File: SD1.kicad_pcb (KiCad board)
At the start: 2 copper layers, 176.1 x 41.3 mm, 236 parts, among them J101 HR861153C, J102 10118194-0001LF, J103 JST ZH 1.5mm 1x5, J107 FPC PMS, J301 PJ-102AH, J302 PJ-102AH, J303 Conn_01x02, J304 Conn_01x02, J401 Conn_01x11, J402 Conn_ARM_JTAG_SWD_10, J403 FTDI_TTL_Cable, J801 Conn_01x02, Q1 FDT86244, Q101 BSS138, Q102 PDTC114EU,115, Q301 DMMT5401, Q302 DMMT5401, Q801 DMMT5401, Q802 DMMT5401, SW103 Multidirection_Switch, SW401 PTS810, T1 HR051067, U102 ER-TFTM028-4, U103 CP2102N-A02-GQFN28R, U104 CC2652P, U105 W5500, U106 EKMC1691111, U107 MCP23017, U108 BME280, U109 SCD30, U2 TPS23753A, U3 TL431A, U301 110-102, U302 LMP91000, U4 TCMT1107, U501 TLV70018, U502 ADPD188BI, U503 Smoke Chamber, U601 CCS811, U701 TPS61022, U702 TLV62585, Y101 25MHz

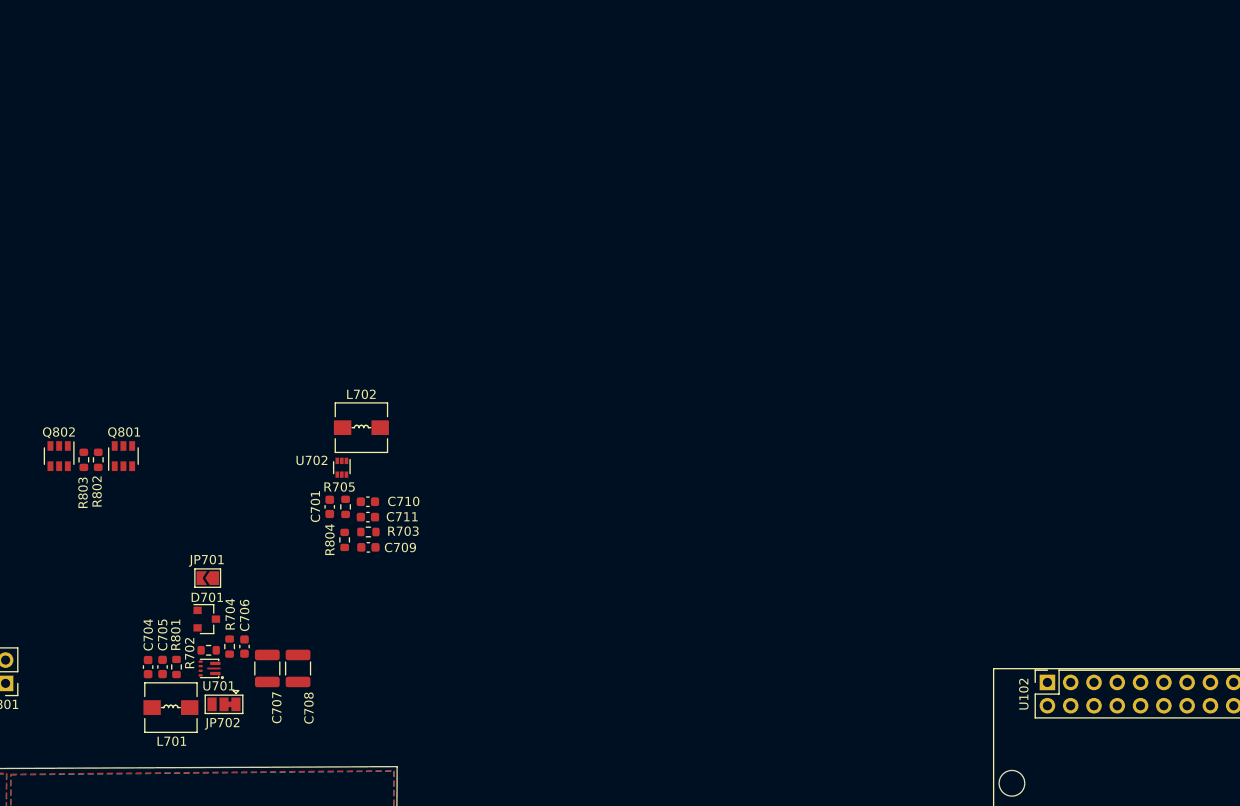
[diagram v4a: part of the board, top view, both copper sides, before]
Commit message: 5V boost and 3.3V buck layout
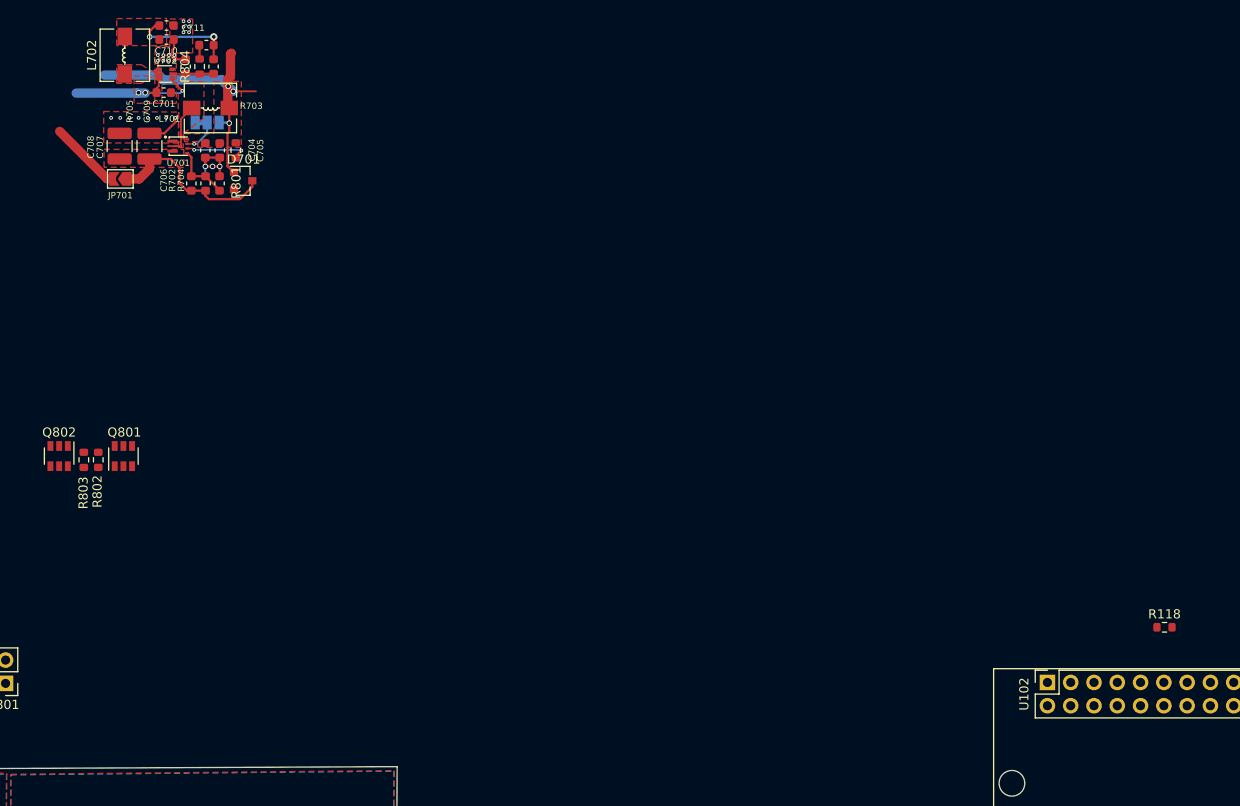
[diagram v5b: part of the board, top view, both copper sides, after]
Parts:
- added R118: 100k, Resistor_SMD:R_0603_1608Metric, F.Cu at (363.9, 42.6)
- JP702: moved to B.Cu
- moved L701 65.5 mm to (259.8, -14.0), turned to 180 degrees
- moved JP702 63.5 mm to (259.5, -12.5), turned to 0 degrees
- moved C708 60.2 mm to (249.9, -9.88), turned to 90 degrees
- moved C707 58.4 mm to (253.2, -9.88), turned to 90 degrees
- moved C711 57.9 mm to (255.0, -23.0), turned to 0 degrees
- moved U701 57.1 mm to (256.3, -9.88), turned to 0 degrees
- moved R801 56.7 mm to (262.6, -9.42), turned to 90 degrees
- moved C704 56.7 mm to (259.3, -9.42), turned to 270 degrees
- moved C705 56.7 mm to (260.9, -9.42), turned to 270 degrees
- moved R703 56.0 mm to (259.4, -20.9)
- moved C709 55.1 mm to (260.2, -18.6), turned to 270 degrees
- moved C710 55.0 mm to (255.0, -21.5), turned to 0 degrees
- moved R804 54.0 mm to (258.7, -18.6)
- moved R705 51.1 mm to (257.1, -18.6), turned to 270 degrees
- moved R702 50.9 mm to (259.3, -5.81), turned to 270 degrees
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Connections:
- U102 pad 29: (no net) -> /LCD_BACKLIGHT
- U102 pad 35: (no net) -> /SD_CS
- U107 pad 1: (no net) -> /SD_CS
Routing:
- net (no net): track 0.00 -> 112.8 mm
- net +BATT: track 0.00 -> 32.3 mm, vias 0 -> 3
- net /Power/5VOUT_BST: track 0.00 -> 19.5 mm
- net GND: track 154.9 -> 171.7 mm, vias 12 -> 37
- net +5V: track 29.8 -> 46.5 mm, vias 0 -> 3
- net +3V3: track 74.7 -> 86.2 mm, vias 3 -> 5
- net Net-(JP701-Pad2): track 0.00 -> 7.81 mm
- net /Power/EN_5V_BST: track 0.00 -> 7.13 mm, vias 0 -> 2
- net Net-(C706-Pad2): track 0.00 -> 6.47 mm
- net /Power/VSW: track 0.00 -> 5.38 mm
- net Net-(C709-Pad2): track 0.00 -> 4.61 mm
- net Net-(JP702-Pad2): track 0.00 -> 3.83 mm, vias 0 -> 1
- net Net-(R703-Pad2): track 0.00 -> 1.57 mm
- added copper zone on F.Cu, net (none)
- added copper zone on F.Cu, net +3V3
- added copper zone on F.Cu, net +BATT
- added copper zone on F.Cu, net /Power/5VOUT_BST
- added copper zone on F.Cu, net /Power/VSW
- added copper zone on F.Cu, net Net-(L702-Pad1)

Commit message: Add resistor to battery indicator, battery layout, update font sizes
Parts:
- added C801: 4.7u, Capacitor_SMD:C_0603_1608Metric, F.Cu at (199.5, 45.2)
- added C802: 4.7u, Capacitor_SMD:C_0603_1608Metric, F.Cu at (192.9, 43.2)
- added D801: LED_ALT, LED_SMD:LED_0603_1608Metric, F.Cu at (195.6, 39.9)
- added D802: LED_ALT, LED_SMD:LED_0603_1608Metric, F.Cu at (195.6, 38.3)
- added J802: Conn_01x02, Connector_JST:JST_PH_B2B-PH-K_1x02_P2.00mm_Vertical, F.Cu at (188.8, 44.2)
- added JP103: Jumper_3_Open, Connector_PinHeader_2.54mm:PinHeader_1x03_P2.54mm_Vertical, F.Cu at (134.2, 178.9)
- added JP801: Jumper_NO_Small, Jumper:SolderJumper-2_P1.3mm_Open_TrianglePad1.0x1.5mm, F.Cu at (203.0, 44.6)
- added R805: 1k, Resistor_SMD:R_0603_1608Metric, F.Cu at (195.6, 36.7)
- added R806: 10k, Resistor_SMD:R_0603_1608Metric, F.Cu at (199.5, 40.0)
- added R807: 1k, Resistor_SMD:R_0603_1608Metric, F.Cu at (198.7, 38.3)
- added U801: MCP73831-2-OT, Package_TO_SOT_SMD:SOT-23-5, F.Cu at (199.1, 42.6)
- moved J801 50.3 mm to (188.4, 37.9), turned to 90 degrees
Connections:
- net /Eth + PoE/PoE Flyback/5V_Main renamed 5V_Main
- Q102 pad 1: (no net) -> /SPKR_Alt
- R109 pad 1: (no net) -> /SPKR
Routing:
- net +BATT: track 32.3 -> 49.9 mm
- net 5V_Main: track 18.4 -> 32.7 mm, vias 2 -> 4
- net Net-(D801-Pad2): track 0.00 -> 5.61 mm
- net Net-(D802-Pad2): track 0.00 -> 2.44 mm
- net Net-(D801-Pad1): track 0.00 -> 2.25 mm
- net Net-(R806-Pad1): track 0.00 -> 1.69 mm
- net Net-(C801-Pad1): track 0.00 -> 1.63 mm

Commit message: Merge layout for PoE and Ethernet
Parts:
- removed MK109, MK110, MK111, MK112: Mounting_Hole_PAD, mylib:MountingHole_3.2mm_M3_ISO14580_Pad
- added D305: BAS16, Diode_SMD:D_SOT-23_ANK, F.Cu at (138.8, 23.2)
- added D306: BAS16, Diode_SMD:D_SOT-23_ANK, F.Cu at (138.8, 26.8)
- added J104: JST 1.25mm, Connector_Molex:Molex_PicoBlade_53398-0871_1x08-1MP_P1.25mm_Vertical, F.Cu at (195.2, 148.8)
- J107: value FPC PMS -> JST 1.25mm
- moved MK101 199.0 mm to (122.8, 10.8)
- moved R807 108.5 mm to (294.1, -13.4)
- moved C801 108.5 mm to (294.9, -6.50)
- moved C802 108.5 mm to (288.3, -8.50)
- moved D801 108.5 mm to (291.0, -11.8)
- moved J801 108.5 mm to (283.8, -13.8)
- moved JP801 108.5 mm to (298.4, -7.10)
- moved R805 108.5 mm to (291.0, -15.0)
- moved R806 108.5 mm to (294.9, -11.7)
- moved U801 108.5 mm to (294.5, -9.10)
- moved J802 108.5 mm to (284.2, -7.50)
- moved D802 108.5 mm to (291.0, -13.4)
- moved C101 105.8 mm to (203.8, 20.3)
- moved C102 105.8 mm to (203.8, 18.7)
- moved D101 105.8 mm to (201.4, 15.0)
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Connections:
- D301 pad 2: /Eth + PoE/PoE Flyback/DC_BARREL -> /Eth + PoE/PoE Flyback/DC_FROM_AC
- D302 pad 2: /Eth + PoE/PoE Flyback/DC_BARREL -> /Eth + PoE/PoE Flyback/DC_FROM_AC
- J301 pad 1: /Eth + PoE/PoE Flyback/DC_BARREL -> /Eth + PoE/PoE Flyback/DC_FROM_AC
- R303 pad 1: /Eth + PoE/PoE Flyback/DC_BARREL -> Net-(D305-Pad1)
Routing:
- net /Eth + PoE/PoE Flyback/VN: track 15.1 -> 55.6 mm
- net /Eth + PoE/PoE Flyback/VP: track 25.9 -> 56.8 mm
- net Net-(D305-Pad1): track 0.00 -> 18.7 mm, vias 0 -> 2
- net /Eth + PoE/PoE Flyback/DC_BARREL: track 0.00 -> 16.6 mm
- net +BATT: track 49.9 -> 36.3 mm, vias 3 -> 1
- net /Eth + PoE/PoE Flyback/DC_FROM_AC: track 0.00 -> 12.0 mm
- net Net-(JP701-Pad2): track 7.81 -> 0.50 mm
- net +5V: track 46.5 -> 39.8 mm
- net /Eth + PoE/ETH_TX_N: track 19.1 -> 24.7 mm
- net /DIO12_RXD: track 27.1 -> 21.7 mm
- net /Eth + PoE/ETH_RX_N: track 29.2 -> 33.5 mm
- net /Eth + PoE/ETH_RX_P: track 32.0 -> 35.8 mm
- net /Eth + PoE/PoE Flyback/APD: track 7.18 -> 5.37 mm, vias 2 -> 1
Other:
- board size 176.1 x 41.3 mm -> 292.9 x 89.5 mm

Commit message: 4layer layout WIP
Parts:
- removed J401: Conn_01x11, Connector_Molex:Molex_SL_171971-0011_1x11_P2.54mm_Vertical
- C802, JP101, JP102: moved to B.Cu
- moved R123 203.1 mm to (97.8, 57.4), turned to 180 degrees
- moved C115 192.3 mm to (88.8, 52.2), turned to 270 degrees
- moved C114 191.5 mm to (210.0, 76.8), turned to 180 degrees
- moved JP401 188.3 mm to (213.4, 18.6), turned to 180 degrees
- moved U109 182.5 mm to (211.0, 74.4), turned to 180 degrees
- moved MK102 169.6 mm to (217.2, 10.8)
- moved SW103 160.1 mm to (122.8, 65.0)
- moved R118 158.0 mm to (212.6, 88.0), turned to 90 degrees
- moved D501 145.6 mm to (139.8, 104.9), turned to 105 degrees
- moved C506 143.7 mm to (152.0, 104.5), turned to 225 degrees
- moved C507 142.9 mm to (150.9, 103.3), turned to 225 degrees
- moved C505 142.2 mm to (149.8, 102.2), turned to 225 degrees
- moved C501 141.0 mm to (149.8, 100.6), turned to 135 degrees
- moved U502 140.4 mm to (153.3, 100.3), turned to 45 degrees
- moved U503 140.3 mm to (153.1, 100.1), turned to 225 degrees
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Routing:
- net (no net): track 112.8 -> 0.00 mm
- net /~ETH_RST: track 0.00 -> 104.1 mm, vias 0 -> 1
- net SPI_MISO: track 4.06 -> 102.5 mm, vias 0 -> 1
- net SPI_MOSI: track 3.04 -> 98.7 mm, vias 0 -> 2
- net SPI_SCK: track 4.69 -> 91.1 mm, vias 0 -> 1
- net /Debug and Serial/WMCU_RTS: track 18.5 -> 70.7 mm, vias 0 -> 1
- net /DIO12_RXD: track 21.7 -> 69.1 mm
- net /Debug and Serial/WMCU_CTS: track 14.2 -> 57.8 mm, vias 1 -> 0
- net /DIO13_TXD: track 18.5 -> 60.5 mm, vias 1 -> 0
- net +5V: track 39.8 -> 68.0 mm, vias 3 -> 11
- net +3V3: track 86.2 -> 112.9 mm, vias 5 -> 6
- net 5V_Main: track 32.7 -> 58.8 mm, vias 4 -> 5
- net +BATT: track 36.3 -> 54.7 mm, vias 1 -> 3
- net GNDA: track 10.5 -> 19.0 mm
- net Net-(J403-Pad3): track 0.00 -> 6.65 mm
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- added copper zone on In1.Cu, net +5V
- added copper zone on In1.Cu, net GND
- added copper zone on F.Cu, net Net-(JP701-Pad2)
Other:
- board size 292.9 x 89.5 mm -> 296.7 x 122.7 mm
- copper layers 2 -> 4
